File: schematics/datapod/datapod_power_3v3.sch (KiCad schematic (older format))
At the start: 12 parts, among them U4 LT8609EMSETRPBF

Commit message: modified schematic
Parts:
- U4: symbol LT8609EMSETRPBF:LT8609EMSETRPBF -> datapod-rescue:LT8609EMSETRPBF-LT8609EMSETRPBF
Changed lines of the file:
@@
 $EndDescr
 $Comp
-L LT8609EMSETRPBF:LT8609EMSETRPBF U4
+L datapod-rescue:LT8609EMSETRPBF-LT8609EMSETRPBF U4
 U 1 1 5E3AFC6C
 P 4150 3300
+AR Path="/5E3AFC6C" Ref="U4"  Part="1"
+AR Path="/5E3AC706/5E3AFC6C" Ref="U4"  Part="1"
 F 0 "U4" H 5150 3700 50  0000 C CNN
 F 1 "LT8609EMSETRPBF" H 5450 3574 50  0000 C CNN

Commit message: added more connectors and started drawing the PCB
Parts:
- removed U4: LT8609EMSETRPBF, Package_SO:MSOP-10-1EP_3x3mm_P0.5mm_EP1.73x1.98mm, symbol datapod-rescue:LT8609EMSETRPBF-LT8609EMSETRPBF
- added U4: LT8609EMSETRPBF, Package_SO:MSOP-10-1EP_3x3mm_P0.5mm_EP1.73x1.98mm, symbol LT8609EMSETRPBF:LT8609EMSETRPBF
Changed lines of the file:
@@
 $EndDescr
-$Comp
-L datapod-rescue:LT8609EMSETRPBF-LT8609EMSETRPBF U4
-U 1 1 5E3AFC6C
-P 4150 3300
-AR Path="/5E3AFC6C" Ref="U4"  Part="1"
-AR Path="/5E3AC706/5E3AFC6C" Ref="U4"  Part="1"
-F 0 "U4" H 5150 3700 50  0000 C CNN
-F 1 "LT8609EMSETRPBF" H 5450 3574 50  0000 C CNN
-F 2 "Package_SO:MSOP-10-1EP_3x3mm_P0.5mm_EP1.73x1.98mm" H 4450 4000 50  0001 L BNN
-F 3 "Linear Technology/Analog" H 4150 3300 50  0001 L BNN
-F 4 "MSOP-10 Linear Technology" H 4450 3900 50  0001 L BNN "Field4"
-F 5 "LT8609/LT8609A/LT8609B - 42V, 2A/3A Peak Synchronous Step-Down Regulator with 2.5μA Quiescent Current" H 4475 3775 50  0001 L BNN "Field5"
-F 6 "LT8609EMSE#TRPBFCT-ND" H 4500 4125 50  0001 L BNN "Field6"
-F 7 "LT8609EMSE#TRPBF" H 4475 4350 50  0001 L BNN "Field7"
-F 8 "https://www.digikey.com/product-detail/en/linear-technology-analog-devices/LT8609EMSE-TRPBF/LT8609EMSE-TRPBFCT-ND/7838162?utm_source=snapeda&utm_medium=aggregator&utm_campaign=symbol" H 4475 4250 50  0001 L BNN "Field8"
-F 9 "LT8609EMSE#TRPBFCT-ND" H 4975 4500 50  0001 C CNN "Part#"
-	1    4150 3300
-	1    0    0    -1
-$EndComp
 $Comp
 L Device:R_US R1
@@
 $EndComp
 $Comp
-L power:GND #PWR0133
+L power:GND #PWR038
 U 1 1 5E3F28CF
 P 6600 2950
-F 0 "#PWR0133" H 6600 2700 50  0001 C CNN
+F 0 "#PWR038" H 6600 2700 50  0001 C CNN
 F 1 "GND" H 6605 2777 50  0000 C CNN
 F 2 "" H 6600 2950 50  0001 C CNN
@@
 	2000 3300 2000 3700
 $Comp
-L power:+3V3 #PWR0134
+L power:+3V3 #PWR036
 U 1 1 5E3F8D06
 P 2000 2400
-F 0 "#PWR0134" H 2000 2250 50  0001 C CNN
+F 0 "#PWR036" H 2000 2250 50  0001 C CNN
 F 1 "+3V3" H 2015 2573 50  0000 C CNN
 F 2 "" H 2000 2400 50  0001 C CNN
@@
 P 7200 2700
 AR Path="/5E40198E" Ref="#PWR?"  Part="1"
-AR Path="/5E3AC706/5E40198E" Ref="#PWR0135"  Part="1"
-F 0 "#PWR0135" H 7200 2550 50  0001 C CNN
+AR Path="/5E3AC706/5E40198E" Ref="#PWR037"  Part="1"
+F 0 "#PWR037" H 7200 2550 50  0001 C CNN
 F 1 "+5V" H 7215 2873 50  0000 C CNN
 F 2 "" H 7200 2700 50  0001 C CNN
@@
 	7000 4700 7000 4950
 $Comp
-L power:GND #PWR0136
+L power:GND #PWR039
 U 1 1 5E3F5404
 P 7000 5400
-F 0 "#PWR0136" H 7000 5150 50  0001 C CNN
+F 0 "#PWR039" H 7000 5150 50  0001 C CNN
 F 1 "GND" H 7005 5227 50  0000 C CNN
 F 2 "" H 7000 5400 50  0001 C CNN
@@
 	6800 4400 3550 4400
 Connection ~ 3550 4400
+$Comp
+L LT8609EMSETRPBF:LT8609EMSETRPBF U4
+U 1 1 5DC5E62C
+P 4150 3300
+F 0 "U4" H 5450 3665 50  0000 C CNN
+F 1 "LT8609EMSETRPBF" H 5450 3574 50  0000 C CNN
+F 2 "Package_SO:MSOP-10-1EP_3x3mm_P0.5mm_EP1.73x1.98mm" H 4450 4000 50  0001 L BNN
+F 3 "Linear Technology/Analog" H 4150 3300 50  0001 L BNN
+F 4 "MSOP-10 Linear Technology" H 4450 3900 50  0001 L BNN "Field4"
+F 5 "LT8609/LT8609A/LT8609B - 42V, 2A/3A Peak Synchronous Step-Down Regulator with 2.5μA Quiescent Current" H 4475 3775 50  0001 L BNN "Field5"
+F 6 "LT8609EMSE#TRPBFCT-ND" H 4500 4125 50  0001 L BNN "Field6"
+F 7 "LT8609EMSE#TRPBF" H 4475 4350 50  0001 L BNN "Field7"
+F 8 "https://www.digikey.com/product-detail/en/linear-technology-analog-devices/LT8609EMSE-TRPBF/LT8609EMSE-TRPBFCT-ND/7838162?utm_source=snapeda&utm_medium=aggregator&utm_campaign=symbol" H 4475 4250 50  0001 L BNN "Field8"
+F 9 "LT8609EMSE#TRPBFCT-ND" H 4975 4500 50  0001 C CNN "Part#"
+	1    4150 3300
+	1    0    0    -1
+$EndComp
 $EndSCHEMATC

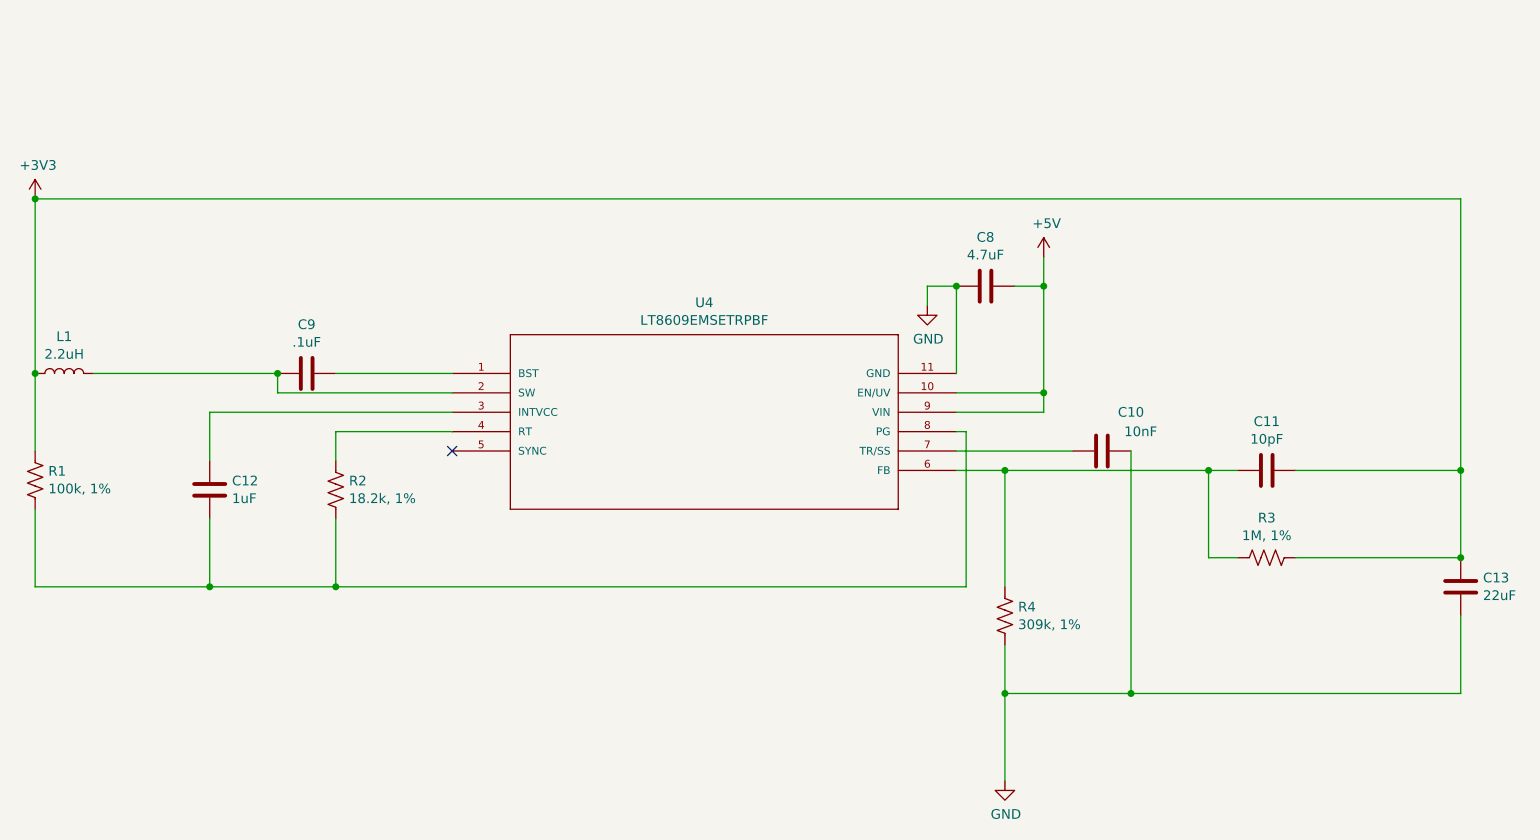
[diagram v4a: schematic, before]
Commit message: fixed bad gnd trace on 3.3v circuit and added comments to the silkscreen
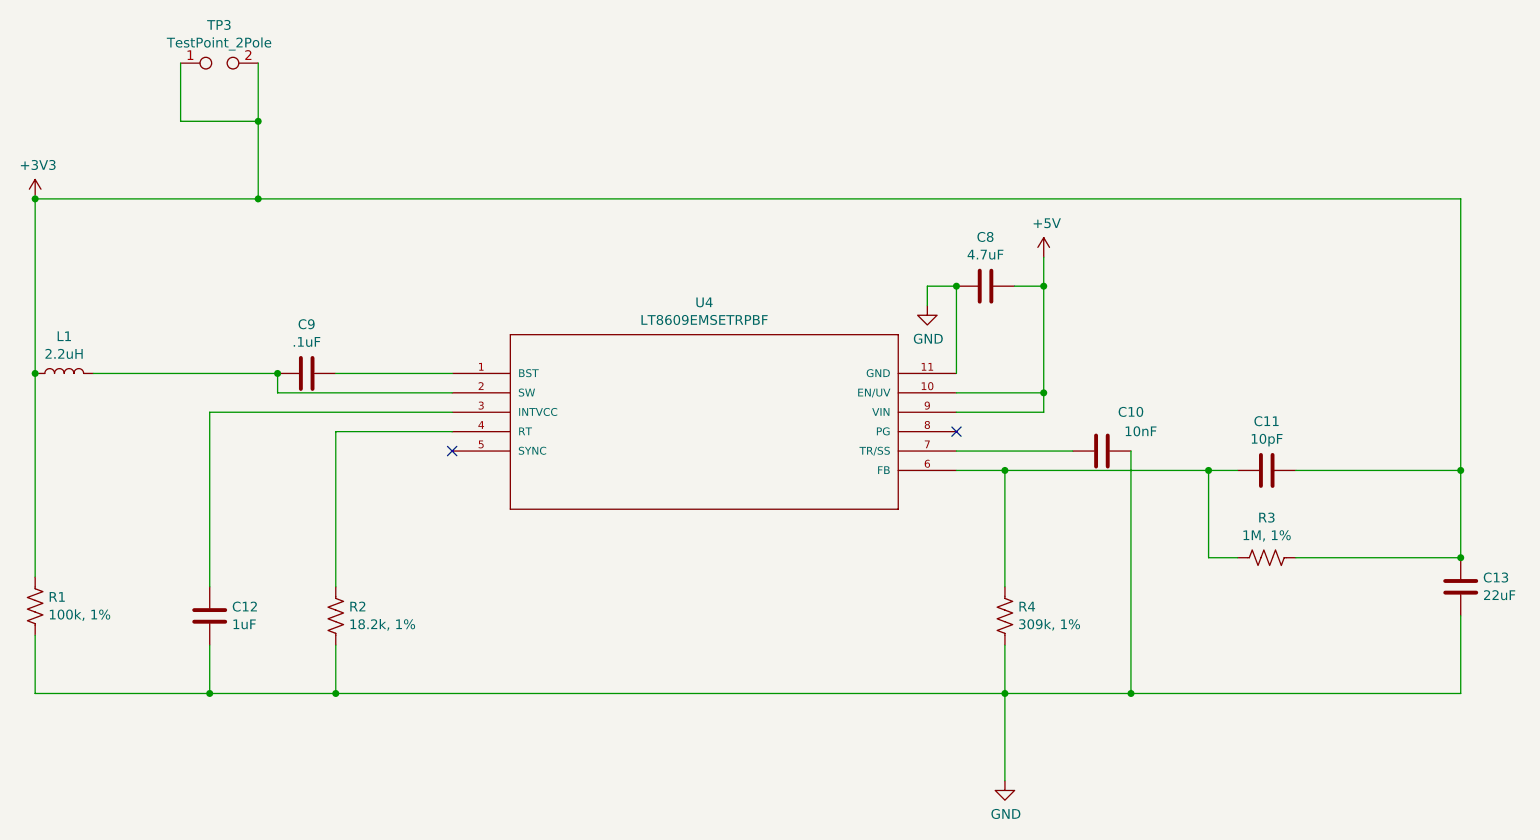
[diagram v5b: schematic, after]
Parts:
- added TP3: TestPoint_2Pole, TestPoint:TestPoint_2Pads_Pitch5.08mm_Drill1.3mm, symbol Connector:TestPoint_2Pole
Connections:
- net +3V3: now also TP3.1, TP3.2
- net GND: now also C12.2, R1.2, R2.2
- now unconnected: U4.8 (PG)
- no-connect marks 1 -> 2
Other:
- moved on the sheet: C12, R1, R2
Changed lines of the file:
@@
 L Device:R_US R1
 U 1 1 5E3B1F9A
-P 2000 3850
-F 0 "R1" H 2068 3896 50  0000 L CNN
-F 1 "100k, 1%" H 2068 3805 50  0000 L CNN
-F 2 "Resistor_SMD:R_0805_2012Metric_Pad1.15x1.40mm_HandSolder" V 2040 3840 50  0001 C CNN
-F 3 "http://www.yageo.com/documents/recent/PYu-RC_Group_51_RoHS_L_10.pdf" H 2000 3850 50  0001 C CNN
-F 4 "Digikey" H 2000 3850 50  0001 C CNN "Vendor"
-F 5 "311-100KCRCT-ND" H 2000 3850 50  0001 C CNN "Part#"
-	1    2000 3850
+P 2000 4500
+F 0 "R1" H 2068 4546 50  0000 L CNN
+F 1 "100k, 1%" H 2068 4455 50  0000 L CNN
+F 2 "Resistor_SMD:R_0805_2012Metric_Pad1.15x1.40mm_HandSolder" V 2040 4490 50  0001 C CNN
+F 3 "http://www.yageo.com/documents/recent/PYu-RC_Group_51_RoHS_L_10.pdf" H 2000 4500 50  0001 C CNN
+F 4 "Digikey" H 2000 4500 50  0001 C CNN "Vendor"
+F 5 "311-100KCRCT-ND" H 2000 4500 50  0001 C CNN "Part#"
+	1    2000 4500
 	1    0    0    -1
 $EndComp
@@
 L Device:R_US R2
 U 1 1 5E3B43B3
-P 3550 3900
-F 0 "R2" H 3618 3946 50  0000 L CNN
-F 1 "18.2k, 1%" H 3618 3855 50  0000 L CNN
-F 2 "Resistor_SMD:R_0805_2012Metric_Pad1.15x1.40mm_HandSolder" V 3590 3890 50  0001 C CNN
-F 3 "http://www.yageo.com/documents/recent/PYu-RC_Group_51_RoHS_L_10.pdf" H 3550 3900 50  0001 C CNN
-F 4 "Digikey" H 3550 3900 50  0001 C CNN "Vendor"
-F 5 "311-18.2KCRCT-ND" H 3550 3900 50  0001 C CNN "Part#"
-	1    3550 3900
+P 3550 4550
+F 0 "R2" H 3618 4596 50  0000 L CNN
+F 1 "18.2k, 1%" H 3618 4505 50  0000 L CNN
+F 2 "Resistor_SMD:R_0805_2012Metric_Pad1.15x1.40mm_HandSolder" V 3590 4540 50  0001 C CNN
+F 3 "http://www.yageo.com/documents/recent/PYu-RC_Group_51_RoHS_L_10.pdf" H 3550 4550 50  0001 C CNN
+F 4 "Digikey" H 3550 4550 50  0001 C CNN "Vendor"
+F 5 "311-18.2KCRCT-ND" H 3550 4550 50  0001 C CNN "Part#"
+	1    3550 4550
 	1    0    0    -1
 $EndComp
@@
 L Device:C C12
 U 1 1 5E3C17C7
-P 2900 3900
-F 0 "C12" H 3015 3946 50  0000 L CNN
-F 1 "1uF" H 3015 3855 50  0000 L CNN
-F 2 "Capacitor_SMD:C_0805_2012Metric_Pad1.15x1.40mm_HandSolder" H 2938 3750 50  0001 C CNN
-F 3 "http://www.yageo.com/documents/recent/UPY-GPHC_X7R_6.3V-to-50V_18.pdf" H 2900 3900 50  0001 C CNN
-F 4 "Digikey" H 2900 3900 50  0001 C CNN "Vendor"
-F 5 "311-1365-1-ND" H 2900 3900 50  0001 C CNN "Part#"
-	1    2900 3900
+P 2900 4550
+F 0 "C12" H 3015 4596 50  0000 L CNN
+F 1 "1uF" H 3015 4505 50  0000 L CNN
+F 2 "Capacitor_SMD:C_0805_2012Metric_Pad1.15x1.40mm_HandSolder" H 2938 4400 50  0001 C CNN
+F 3 "http://www.yageo.com/documents/recent/UPY-GPHC_X7R_6.3V-to-50V_18.pdf" H 2900 4550 50  0001 C CNN
+F 4 "Digikey" H 2900 4550 50  0001 C CNN "Vendor"
+F 5 "311-1365-1-ND" H 2900 4550 50  0001 C CNN "Part#"
+	1    2900 4550
 	1    0    0    -1
 $EndComp
@@
 	3250 3300 2300 3300
 Connection ~ 3250 3300
-Wire Wire Line
-	2000 3300 2000 3700
 $Comp
 L power:+3V3 #PWR036
@@
 Wire Wire Line
 	4150 3500 2900 3500
-Wire Wire Line
-	2900 3500 2900 3750
-Wire Wire Line
-	2000 4000 2000 4400
-Wire Wire Line
-	2000 4400 2900 4400
-Wire Wire Line
-	2900 4400 2900 4050
-Wire Wire Line
-	2900 4400 3550 4400
-Wire Wire Line
-	3550 4400 3550 4050
-Connection ~ 2900 4400
-Wire Wire Line
-	3550 3600 3550 3750
 Wire Wire Line
 	3550 3600 4150 3600
@@
 Connection ~ 9350 4250
 Wire Wire Line
-	9350 2400 2000 2400
+	9350 2400 3150 2400
 Connection ~ 2000 2400
 Wire Wire Line
@@
 	6600 2850 6600 2950
 Connection ~ 6750 2850
-Wire Wire Line
-	6750 3600 6800 3600
-Wire Wire Line
-	6800 3600 6800 4400
-Wire Wire Line
-	6800 4400 3550 4400
-Connection ~ 3550 4400
 $Comp
 L LT8609EMSETRPBF:LT8609EMSETRPBF U4
@@
 	1    0    0    -1
 $EndComp
+NoConn ~ 6750 3600
+Wire Wire Line
+	2000 3300 2000 4350
+Wire Wire Line
+	2000 4650 2000 4950
+Wire Wire Line
+	7000 4950 3550 4950
+Wire Wire Line
+	2900 4700 2900 4950
+Connection ~ 2900 4950
+Wire Wire Line
+	2900 4950 2000 4950
+Wire Wire Line
+	3550 4700 3550 4950
+Connection ~ 3550 4950
+Wire Wire Line
+	3550 4950 2900 4950
+Wire Wire Line
+	3550 3600 3550 4400
+Wire Wire Line
+	2900 3500 2900 4400
+$Comp
+L Connector:TestPoint_2Pole TP3
+U 1 1 5E2794A0
+P 2950 1700
+F 0 "TP3" H 2950 1895 50  0000 C CNN
+F 1 "TestPoint_2Pole" H 2950 1804 50  0000 C CNN
+F 2 "TestPoint:TestPoint_2Pads_Pitch5.08mm_Drill1.3mm" H 2950 1700 50  0001 C CNN
+F 3 "~" H 2950 1700 50  0001 C CNN
+	1    2950 1700
+	1    0    0    -1
+$EndComp
+Wire Wire Line
+	3150 1700 3150 2000
+Connection ~ 3150 2400
+Wire Wire Line
+	3150 2400 2000 2400
+Wire Wire Line
+	2750 1700 2750 2000
+Wire Wire Line
+	2750 2000 3150 2000
+Connection ~ 3150 2000
+Wire Wire Line
+	3150 2000 3150 2400
 $EndSCHEMATC

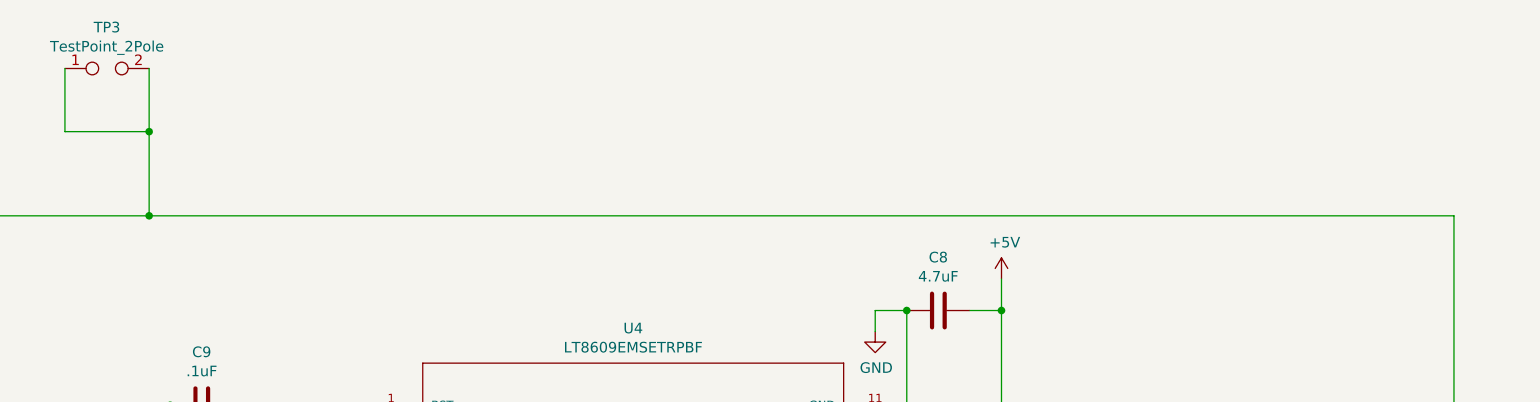
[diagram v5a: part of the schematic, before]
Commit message: added rtc stuff , rotated db9s , added on/off transistors for max chip and sdcard
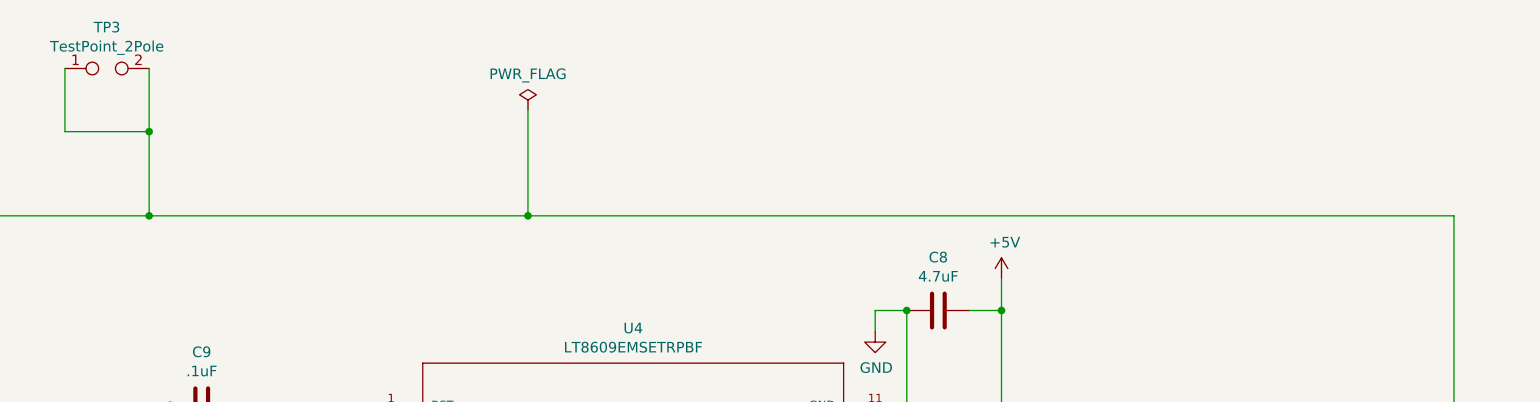
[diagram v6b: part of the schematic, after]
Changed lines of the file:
@@
 Connection ~ 9350 4250
 Wire Wire Line
-	9350 2400 3150 2400
+	9350 2400 4950 2400
 Connection ~ 2000 2400
 Wire Wire Line
@@
 Wire Wire Line
 	3150 2000 3150 2400
+$Comp
+L power:PWR_FLAG #FLG0110
+U 1 1 5E2D38AC
+P 4950 1900
+F 0 "#FLG0110" H 4950 1975 50  0001 C CNN
+F 1 "PWR_FLAG" H 4950 2073 50  0000 C CNN
+F 2 "" H 4950 1900 50  0001 C CNN
+F 3 "~" H 4950 1900 50  0001 C CNN
+	1    4950 1900
+	1    0    0    -1
+$EndComp
+Wire Wire Line
+	4950 1900 4950 2400
+Connection ~ 4950 2400
+Wire Wire Line
+	4950 2400 3150 2400
 $EndSCHEMATC

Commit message: rev 3 , moved db9 connectors out and added ajumper to change output to 14.4v
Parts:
- TP3: Part# (none) -> DNI
- U4: Field4 MSOP-10 Linear Technology -> (none); Field5 LT8609/LT8609A/LT8609B - 42V, 2A/3A Peak Synchronous Step-D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 -> (none); Field6 LT8609EMSE#TRPBFCT-ND -> (none); Field7 LT8609EMSE#TRPBF -> (none); Field8 https://www.digikey.com/product-detail/en/linear-technology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 -> (none); Vendor (none) -> Digikey
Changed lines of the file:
@@
 F 1 "LT8609EMSETRPBF" H 5450 3574 50  0000 C CNN
 F 2 "Package_SO:MSOP-10-1EP_3x3mm_P0.5mm_EP1.73x1.98mm" H 4450 4000 50  0001 L BNN
-F 3 "Linear Technology/Analog" H 4150 3300 50  0001 L BNN
-F 4 "MSOP-10 Linear Technology" H 4450 3900 50  0001 L BNN "Field4"
-F 5 "LT8609/LT8609A/LT8609B - 42V, 2A/3A Peak Synchronous Step-Down Regulator with 2.5μA Quiescent Current" H 4475 3775 50  0001 L BNN "Field5"
-F 6 "LT8609EMSE#TRPBFCT-ND" H 4500 4125 50  0001 L BNN "Field6"
-F 7 "LT8609EMSE#TRPBF" H 4475 4350 50  0001 L BNN "Field7"
-F 8 "https://www.digikey.com/product-detail/en/linear-technology-analog-devices/LT8609EMSE-TRPBF/LT8609EMSE-TRPBFCT-ND/7838162?utm_source=snapeda&utm_medium=aggregator&utm_campaign=symbol" H 4475 4250 50  0001 L BNN "Field8"
-F 9 "LT8609EMSE#TRPBFCT-ND" H 4975 4500 50  0001 C CNN "Part#"
+F 3 "https://www.analog.com/media/en/technical-documentation/data-sheets/LT8609-8609A-8609B.pdf" H 4150 3300 50  0001 L BNN
+F 4 "Digikey" H 4150 3300 50  0001 C CNN "Vendor"
+F 5 "LT8609EMSE#TRPBFCT-ND" H 4975 4500 50  0001 C CNN "Part#"
 	1    4150 3300
 	1    0    0    -1
@@
 F 2 "TestPoint:TestPoint_2Pads_Pitch5.08mm_Drill1.3mm" H 2950 1700 50  0001 C CNN
 F 3 "~" H 2950 1700 50  0001 C CNN
+F 4 "DNI" H 2950 1700 50  0001 C CNN "Part#"
 	1    2950 1700
 	1    0    0    -1
